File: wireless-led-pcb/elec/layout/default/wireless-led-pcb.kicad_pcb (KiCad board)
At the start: 4 copper layers, 154 x 30 mm, 48 parts

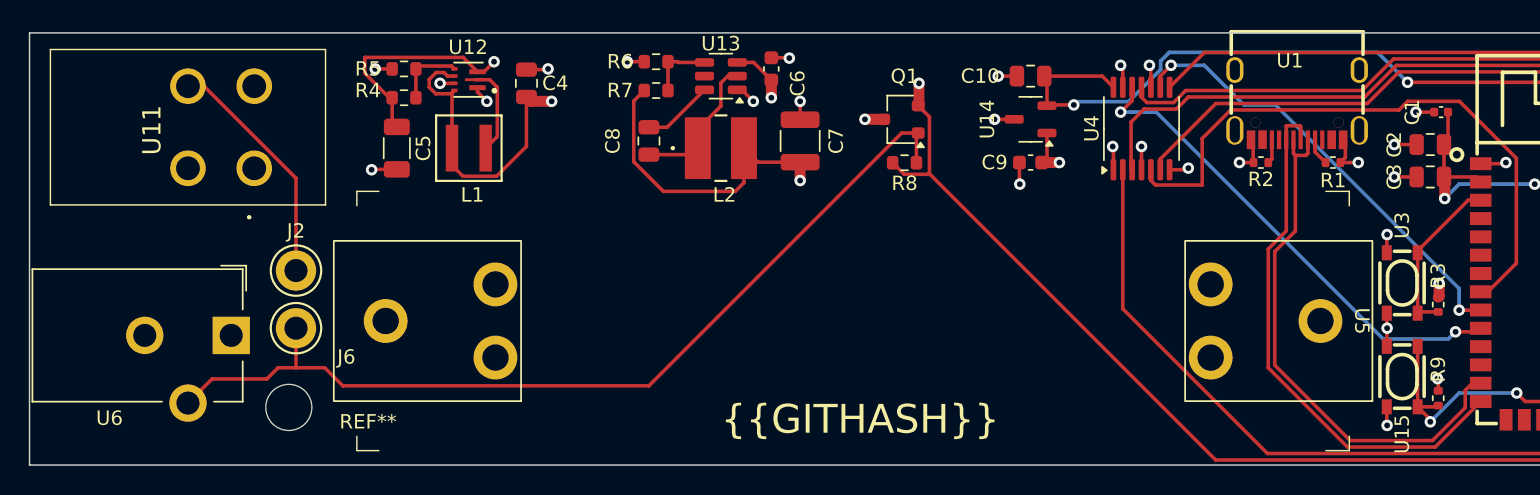
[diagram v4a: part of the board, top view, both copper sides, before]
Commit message: removed the high side switch and added a jumper for disconnecting the battery.
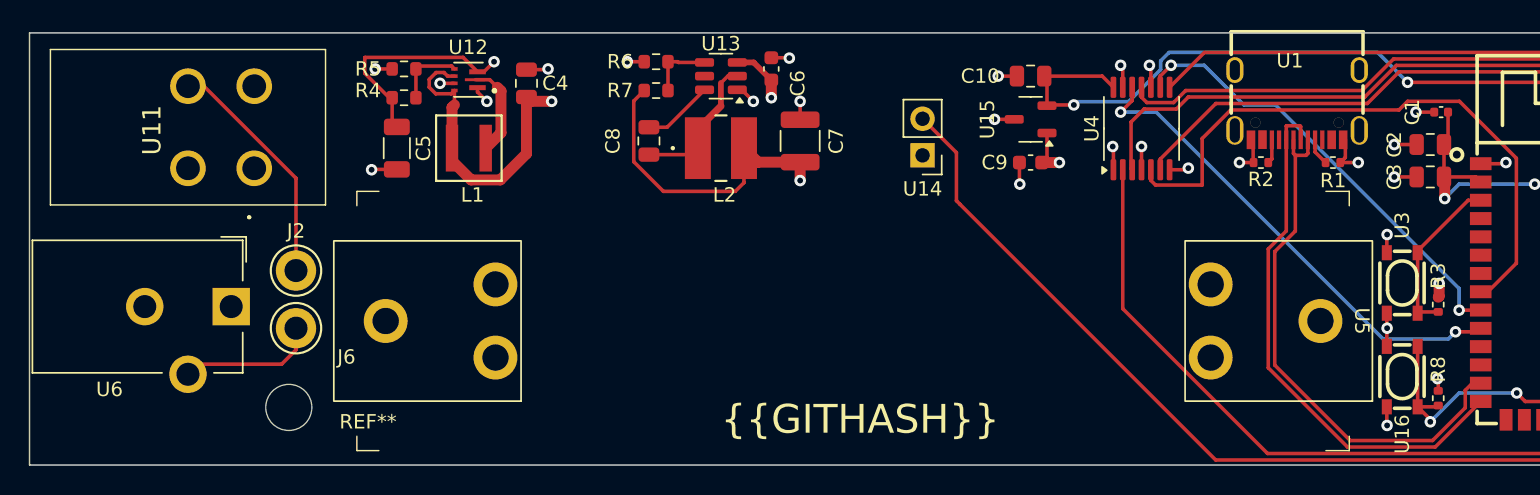
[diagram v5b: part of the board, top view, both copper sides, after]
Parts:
- removed Q1: , Package_TO_SOT_SMD:SC-59
- removed the R8 at (90.8, 79.0)
- added U14: , Connector_PinHeader_2.54mm:PinHeader_1x02_P2.54mm_Vertical, F.Cu at (92.0, 78.5)
- moved U6 2.00 mm to (44.0, 89.0)
- renumbered R9 to R8, U14 to U15, U15 to U16
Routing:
- net detect: track 64.4 -> 9.70 mm
- net boost_3v7_to_5v-vcc: track 165.9 -> 163.0 mm, vias 2 -> 1
- net barrel_jack-vcc: track 12.8 -> 10.8 mm
- net led_strip_connector_1-vcc: track 200.2 -> 198.9 mm, vias 3 -> 2
